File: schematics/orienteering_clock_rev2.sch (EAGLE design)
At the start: 60 parts, among them IC1 TPIC6B595N, IC2 TPIC6B595N, J2 ICSP, Q1 IRFU9024V, Q2 IRFU9024V, Q3 IRFU9024V, Q4 IRFU9024V, Q5 IRFU9024V, Q6 IRFU9024V, T1 BC547, Y1 16MHz

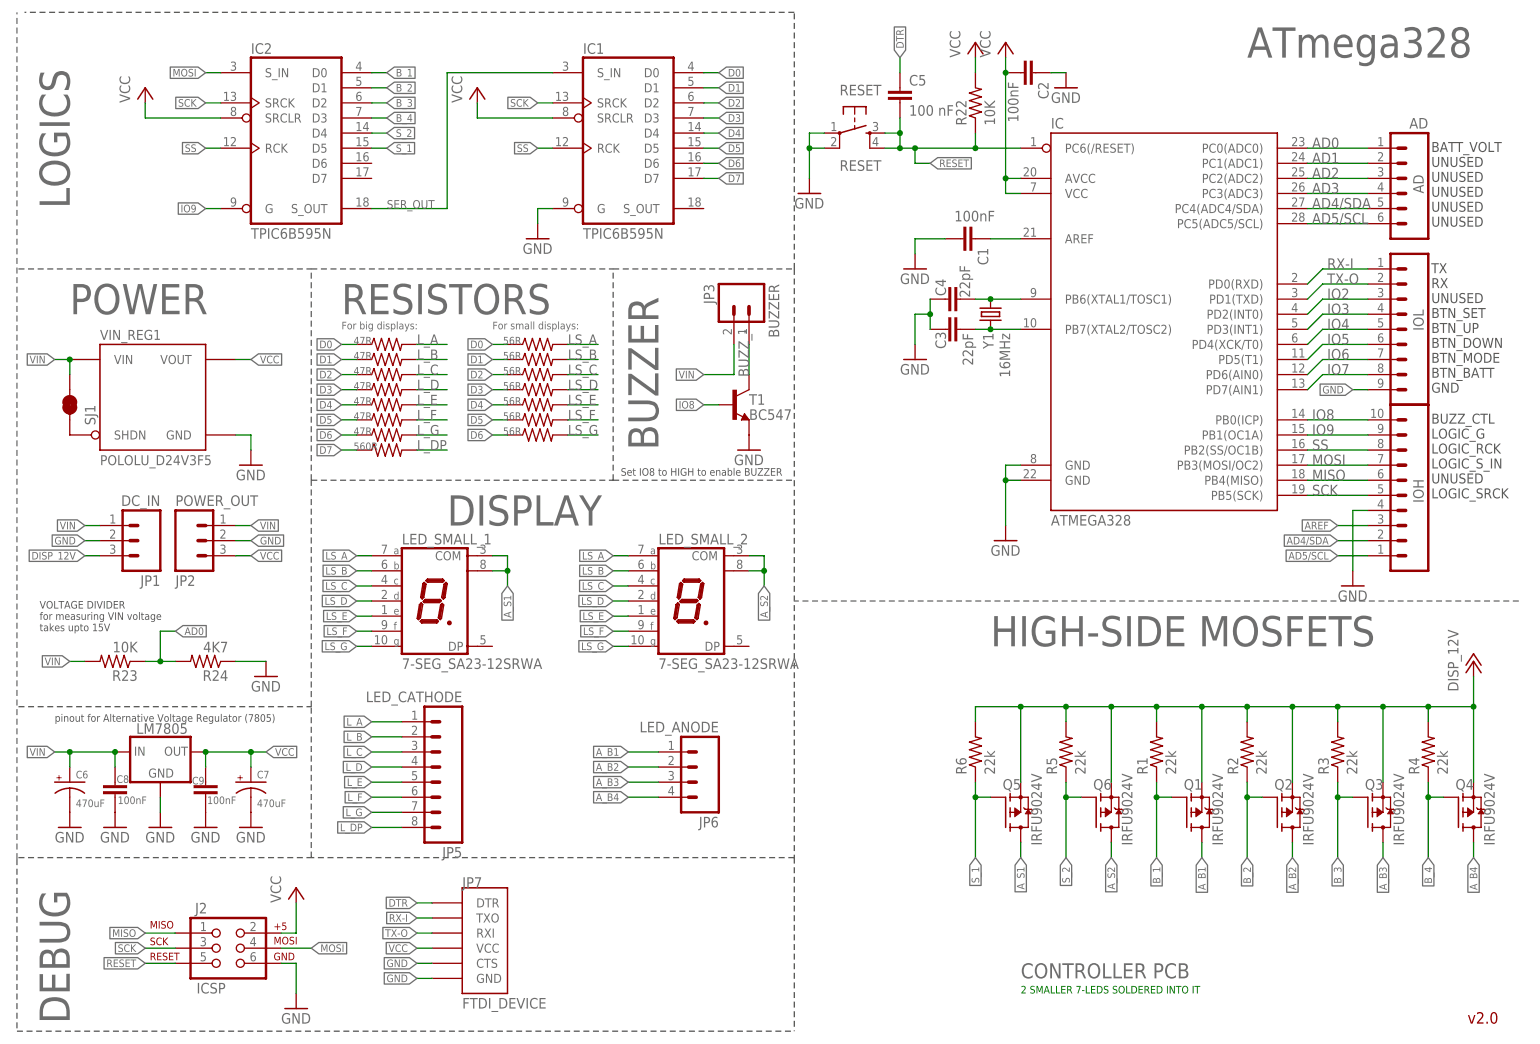
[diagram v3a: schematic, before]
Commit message: schematics: inverted small displays bug, revision 2.1
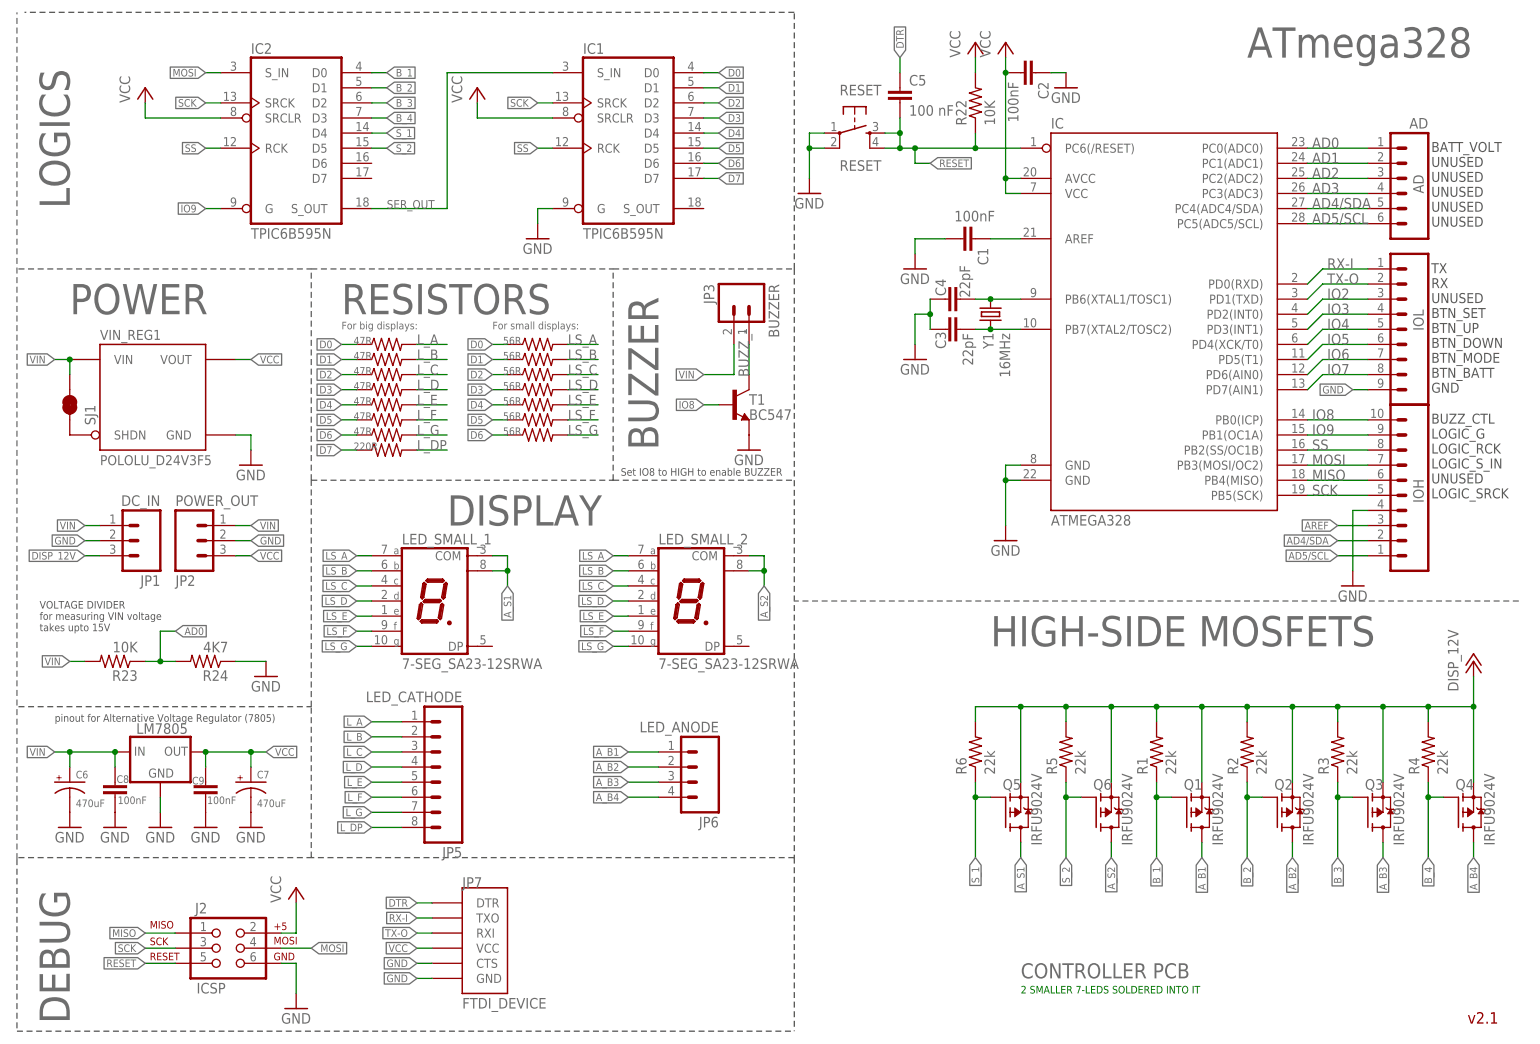
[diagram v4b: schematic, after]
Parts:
- R21: value 560R -> 220R
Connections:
- net S_1: now also IC2A.D4; no longer IC2A.D5
- net S_2: now also IC2A.D5; no longer IC2A.D4
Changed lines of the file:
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@@
 <schematic xreflabel="%F%N/%S.%C%R" xrefpart="/%S.%C%R">
 <attributes>
-<attribute name="REVISION" value="v2.0"/>
+<attribute name="REVISION" value="v2.1"/>
 </attributes>
 <variantdefs>
@@
 <part name="JP5" library="SparkFun-Connectors" deviceset="M08" device="" value="LED_CATHODE"/>
 <part name="JP6" library="SparkFun-Connectors" deviceset="M04" device="PTH" value="LED_ANODE"/>
-<part name="R21" library="resistor" deviceset="R-US_" device="0207/10" value="560R"/>
+<part name="R21" library="resistor" deviceset="R-US_" device="0207/10" value="220R"/>
 <part name="JP7" library="SparkFun-Connectors" deviceset="FTDI_DEVICE" device=""/>
 <part name="R23" library="resistor" deviceset="R-US_" device="0207/10" value="10K"/>
@@
 <net name="S_1" class="0">
 <segment>
-<pinref part="IC2" gate="A" pin="D5"/>
-<wire x1="12.7" y1="104.14" x2="15.24" y2="104.14" width="0.1524" layer="91"/>
-<label x="15.24" y="104.14" size="1.27" layer="95" xref="yes"/>
-</segment>
-<segment>
 <pinref part="Q5" gate="G$1" pin="G"/>
 <wire x1="116.84" y1="-5.08" x2="114.3" y2="-5.08" width="0.1524" layer="91"/>
@@
 <label x="114.3" y="-15.24" size="1.27" layer="95" rot="R270" xref="yes"/>
 </segment>
-</net>
-<net name="S_2" class="0">
 <segment>
 <pinref part="IC2" gate="A" pin="D4"/>
@@
 <label x="15.24" y="106.68" size="1.27" layer="95" xref="yes"/>
 </segment>
+</net>
+<net name="S_2" class="0">
 <segment>
 <pinref part="Q6" gate="G$1" pin="G"/>
@@
 <label x="129.54" y="-15.24" size="1.27" layer="95" rot="R270" xref="yes"/>
 </segment>
-</net>
+<segment>
+<pinref part="IC2" gate="A" pin="D5"/>
+<wire x1="12.7" y1="104.14" x2="15.24" y2="104.14" width="0.1524" layer="91"/>
+<label x="15.24" y="104.14" size="1.27" layer="95" xref="yes"/>
+</segment>
+</net>
